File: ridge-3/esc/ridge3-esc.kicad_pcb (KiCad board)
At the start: 6 copper layers, 33.8 x 33.8 mm, 171 parts, among them Q1A AON7934, Q1B AON7934, Q1C AON7934, Q2A AON7934, Q2B AON7934, Q2C AON7934, Q3A AON7934, Q3B AON7934, Q3C AON7934, Q4A AON7934, Q4B AON7934, Q4C AON7934

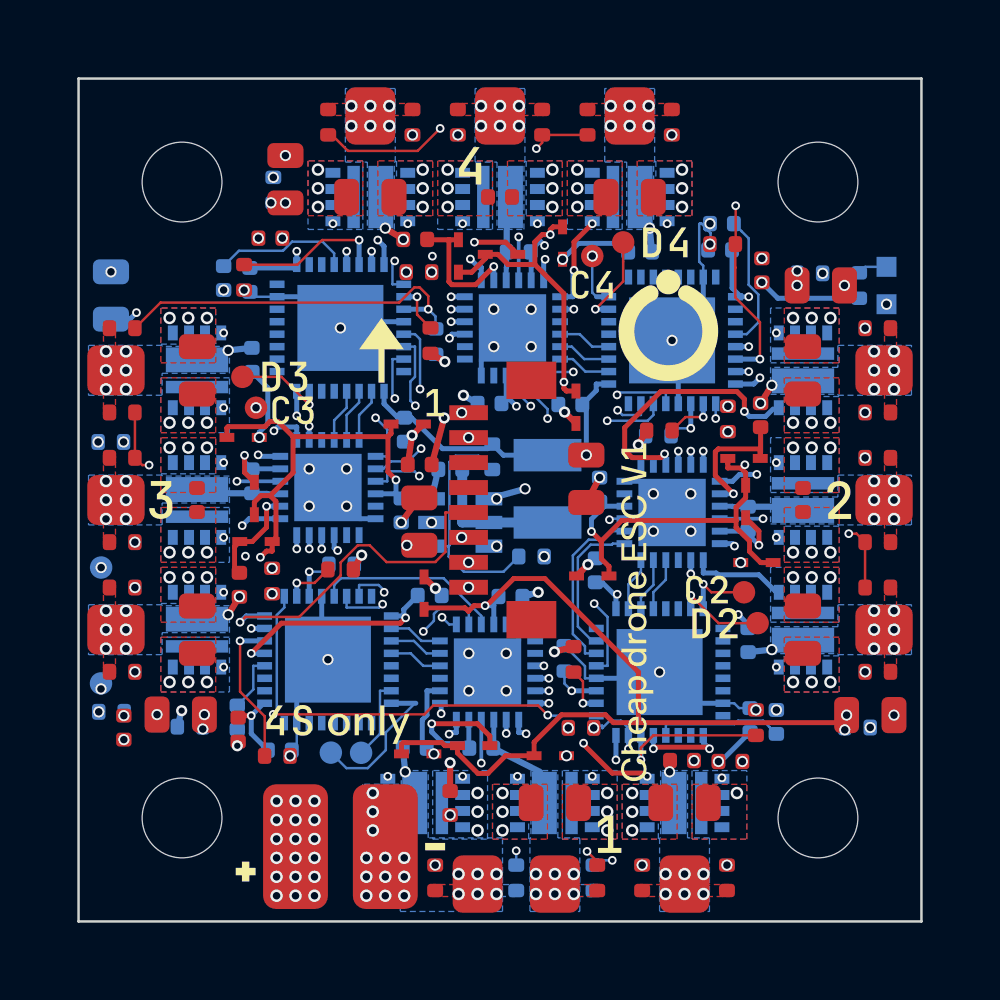
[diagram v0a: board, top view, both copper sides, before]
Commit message: ESC routed to DRC 0/0/0 and installed; panel fiducial check reads real extents
The deterministic run (pipeline.run 'esc', seed as committed) routed the
channel template with 0 nets open, stamped it onto all four channels with
every copy kept, and Freerouting finished the whole board with nothing
left: DRC 0 errors, 0 warnings, 0 unconnected with the silkscreen on.
Installed as esc/ridge3-esc.kicad_pcb with its outputs; the old
cheapdrone-esc images, production files and STEP are gone.

The panel's fiducial keep-out check sized an aperture macro by its
largest parameter; a free-polygon pad's first parameter is its rotation,
so a pad turned 180 degrees counted as a 180 mm disc and "covered" every
bottom fiducial. It now measures each object's real extent (gerbonara
evaluates the macro): region outlines, else bounding boxes.

The ESC's firmware name (RIDGE3_G071) found no room on top; it now goes
on the bottom when the top has none.

Co-Authored-By: Claude Opus 5.5 <noreply@anthropic.com>
Claude-Session: https://claude.ai/code/session_01MaVFAzoExts7u2gmCraXFC
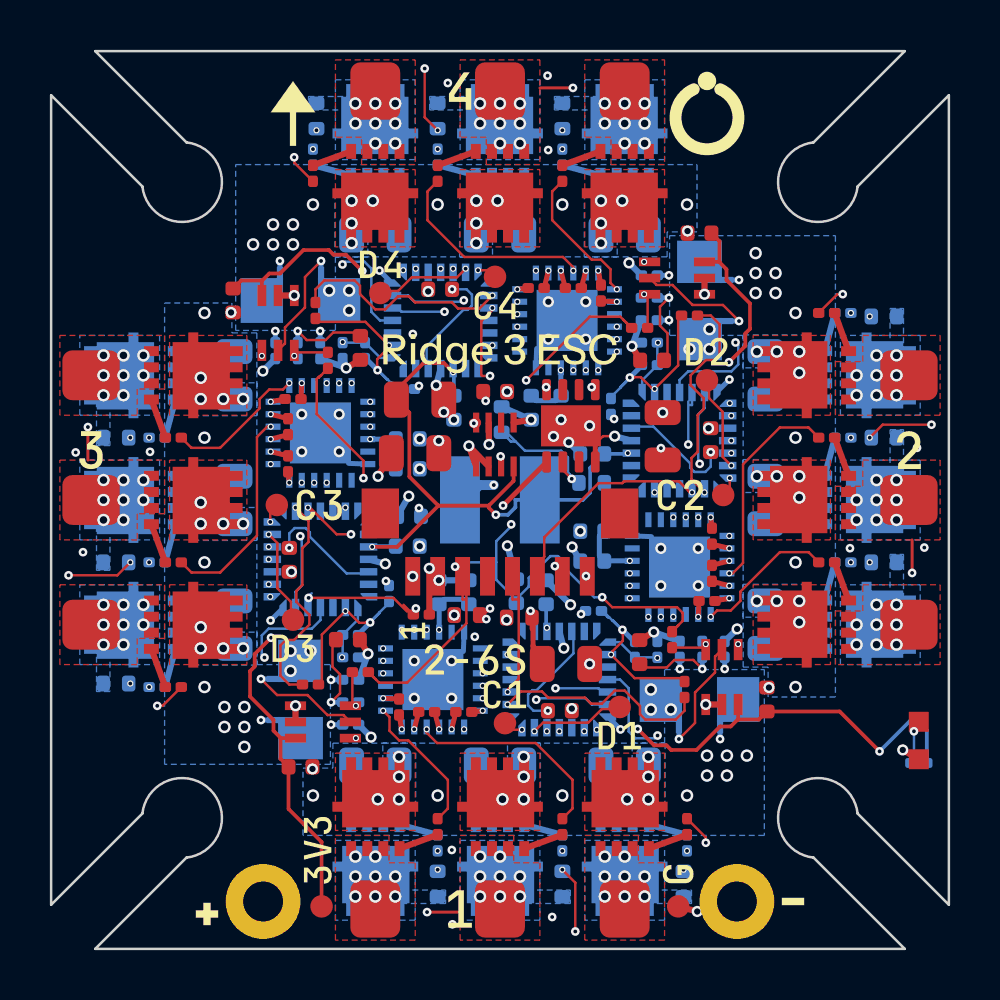
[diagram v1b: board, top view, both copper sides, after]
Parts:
- removed D1, D13, D5, D9: 15V, SOD-523_L1.2-W0.8-LS1.6-RD
- removed D10, D11, D12, D14, D15, D16, D2, D3, D4, D6, D7, D8: RB521S30, SOD-523_L1.2-W0.8-LS1.6-RD
- removed the LED_PWR at (115.5, 91.4)
- removed Q1A, Q1B, Q1C, Q2A, Q2B, Q2C, Q3A, Q3B, Q3C, Q4A, Q4B, Q4C: AON7934, DFN-8_L3.0-W3.0-P0.65-BL_AON7934
- removed the U_BUCK at (98.4, 100.9)
- added C55: 100nF, C_0402_1005Metric, F.Cu at (94.4, 93.9)
- added LED_PWR: RED, LED0603-RD, F.Cu at (116.8, 109.6)
- added Q1AH: TPN2R304PL, TSON-8_L3.1-W3.1-P0.65-LS3.3-BL-EP, F.Cu at (95.0, 112.3)
- added Q1AL: TPN2R304PL, TSON-8_L3.1-W3.1-P0.65-LS3.3-BL-EP, B.Cu at (95.0, 114.7)
- added Q1BH: TPN2R304PL, TSON-8_L3.1-W3.1-P0.65-LS3.3-BL-EP, F.Cu at (100.0, 112.3)
- added Q1BL: TPN2R304PL, TSON-8_L3.1-W3.1-P0.65-LS3.3-BL-EP, B.Cu at (100.0, 114.7)
- added Q1CH: TPN2R304PL, TSON-8_L3.1-W3.1-P0.65-LS3.3-BL-EP, F.Cu at (105.0, 112.3)
- added Q1CL: TPN2R304PL, TSON-8_L3.1-W3.1-P0.65-LS3.3-BL-EP, B.Cu at (105.0, 114.7)
- added Q2AH: TPN2R304PL, TSON-8_L3.1-W3.1-P0.65-LS3.3-BL-EP, F.Cu at (112.3, 105.0)
- added Q2AL: TPN2R304PL, TSON-8_L3.1-W3.1-P0.65-LS3.3-BL-EP, B.Cu at (114.7, 105.0)
- added Q2BH: TPN2R304PL, TSON-8_L3.1-W3.1-P0.65-LS3.3-BL-EP, F.Cu at (112.3, 100.0)
- added Q2BL: TPN2R304PL, TSON-8_L3.1-W3.1-P0.65-LS3.3-BL-EP, B.Cu at (114.7, 100.0)
- added Q2CH: TPN2R304PL, TSON-8_L3.1-W3.1-P0.65-LS3.3-BL-EP, F.Cu at (112.3, 95.0)
- added Q2CL: TPN2R304PL, TSON-8_L3.1-W3.1-P0.65-LS3.3-BL-EP, B.Cu at (114.7, 95.0)
- added Q3AH: TPN2R304PL, TSON-8_L3.1-W3.1-P0.65-LS3.3-BL-EP, F.Cu at (87.7, 95.0)
- added Q3AL: TPN2R304PL, TSON-8_L3.1-W3.1-P0.65-LS3.3-BL-EP, B.Cu at (85.3, 95.0)
- added Q3BH: TPN2R304PL, TSON-8_L3.1-W3.1-P0.65-LS3.3-BL-EP, F.Cu at (87.7, 100.0)
- added Q3BL: TPN2R304PL, TSON-8_L3.1-W3.1-P0.65-LS3.3-BL-EP, B.Cu at (85.3, 100.0)
- added Q3CH: TPN2R304PL, TSON-8_L3.1-W3.1-P0.65-LS3.3-BL-EP, F.Cu at (87.7, 105.0)
- added Q3CL: TPN2R304PL, TSON-8_L3.1-W3.1-P0.65-LS3.3-BL-EP, B.Cu at (85.3, 105.0)
- added Q4AH: TPN2R304PL, TSON-8_L3.1-W3.1-P0.65-LS3.3-BL-EP, F.Cu at (105.0, 87.7)
- added Q4AL: TPN2R304PL, TSON-8_L3.1-W3.1-P0.65-LS3.3-BL-EP, B.Cu at (105.0, 85.3)
- added Q4BH: TPN2R304PL, TSON-8_L3.1-W3.1-P0.65-LS3.3-BL-EP, F.Cu at (100.0, 87.7)
- added Q4BL: TPN2R304PL, TSON-8_L3.1-W3.1-P0.65-LS3.3-BL-EP, B.Cu at (100.0, 85.3)
- added Q4CH: TPN2R304PL, TSON-8_L3.1-W3.1-P0.65-LS3.3-BL-EP, F.Cu at (95.0, 87.7)
- added Q4CL: TPN2R304PL, TSON-8_L3.1-W3.1-P0.65-LS3.3-BL-EP, B.Cu at (95.0, 85.3)
- added R50: 20k, R_0402_1005Metric, B.Cu at (84.6, 102.5)
- added R51: 2k, R_0201_0603Metric, B.Cu at (94.0, 109.0)
- added R52: 10k, R_0201_0603Metric, F.Cu at (92.4, 107.4)
- added R53: 10R, R_0201_0603Metric, F.Cu at (86.9, 107.5)
- added R54: 10R, R_0201_0603Metric, B.Cu at (86.2, 107.5)
- added R55: 20k, R_0402_1005Metric, B.Cu at (84.6, 107.4)
- added R56: 2k, R_0201_0603Metric, B.Cu at (94.0, 106.3)
- added R57: 10k, R_0201_0603Metric, B.Cu at (94.0, 105.4)
- added R58: 1k, R_0201_0603Metric, B.Cu at (94.0, 108.1)
- added R59: 10R, R_0201_0603Metric, F.Cu at (102.5, 86.9)
- added R60: 10R, R_0201_0603Metric, B.Cu at (102.5, 86.2)
- added R61: 20k, R_0402_1005Metric, B.Cu at (102.5, 84.6)
- added R62: 2k, R_0201_0603Metric, B.Cu at (92.8, 94.0)
- added R63: 10k, R_0201_0603Metric, B.Cu at (96.2, 95.5)
- added R64: 10R, R_0201_0603Metric, F.Cu at (97.5, 86.9)
- added R65: 10R, R_0201_0603Metric, B.Cu at (97.5, 86.2)
- added R66: 20k, R_0402_1005Metric, B.Cu at (97.5, 84.6)
- added R67: 2k, R_0201_0603Metric, B.Cu at (91.0, 94.0)
- added R68: 10k, R_0201_0603Metric, F.Cu at (92.6, 92.4)
- added R69: 10R, R_0201_0603Metric, F.Cu at (92.5, 86.9)
- added R70: 10R, R_0201_0603Metric, B.Cu at (92.5, 86.2)
- added R71: 20k, R_0402_1005Metric, B.Cu at (92.6, 84.6)
- added R72: 2k, R_0201_0603Metric, B.Cu at (93.7, 94.0)
- added R73: 10k, R_0201_0603Metric, B.Cu at (94.6, 94.0)
- added R74: 1k, R_0201_0603Metric, B.Cu at (91.9, 94.0)
- added R_SH1: 0.5mR, RES-SMD_1206_HCS1206, B.Cu at (108.0, 108.0)
- added R_SH2: 0.5mR, RES-SMD_1206_HCS1206, B.Cu at (108.0, 92.0)
- added R_SH3: 0.5mR, RES-SMD_1206_HCS1206, B.Cu at (92.0, 108.0)
- added R_SH4: 0.5mR, RES-SMD_1206_HCS1206, B.Cu at (92.0, 92.0)
- added U_BUCK: MAX15062A 3.3V, TDFN-8_L2.0-W2.0-P0.50-BL_MAX15062AATA, F.Cu at (99.8, 97.8)
- added U_CS1: INA186A3, SC-70-6_L2.0-W1.3-P0.65-LS2.1-BL, F.Cu at (108.9, 107.1)
- added U_CS2: INA186A3, SC-70-6_L2.0-W1.3-P0.65-LS2.1-BL, F.Cu at (107.1, 91.1)
- added U_CS3: INA186A3, SC-70-6_L2.0-W1.3-P0.65-LS2.1-BL, F.Cu at (92.9, 108.9)
- added U_CS4: INA186A3, SC-70-6_L2.0-W1.3-P0.65-LS2.1-BL, F.Cu at (91.1, 92.9)
- added U_GVDD: TPS7A1601, VSON-8-1EP_3x3mm_P0.65mm_EP1.65x2.4mm, F.Cu at (102.8, 97.0)
- C1, C11, C23, C35, C47: value 10uF -> 100nF; footprint C_0805_2012Metric -> C_0402_1005Metric; moved to B.Cu
- C10, C22, C34, C46: value 100nF -> 1uF
- C12, C24, C36, C48: value 100nF -> 1uF; footprint C_0402_1005Metric -> C_0201_0603Metric; moved to F.Cu
- C13, C25, C37, C49: value 1uF -> 4.7uF; footprint C_0402_1005Metric -> C_0805_2012Metric
- C14, C26, C38, C50: footprint C_0402_1005Metric -> C_0201_0603Metric; moved to F.Cu
- C15, C27, C39, C51: value 1uF -> 4.7uF; footprint C_0402_1005Metric -> C_0805_2012Metric; moved to B.Cu
- C16, C28, C40, C52: value 10uF -> 1uF; footprint C_0805_2012Metric -> C_0201_0603Metric
- C17, C29, C41, C53: value 10uF -> 4.7uF; moved to B.Cu
- C19, C31, C43, TP_3V3, TP_E1_CLK, TP_E1_DIO, TP_GND: moved to F.Cu
- C2: value 100nF -> 1uF; footprint C_0402_1005Metric -> C_0805_2012Metric
- C20, C32, C44, C8: value 4.7uF -> 100nF
- C21, C33, C45, C9: value 1uF -> 100nF
- C3: value 100nF -> 1uF; moved to F.Cu
- C4: value 22uF -> 10uF
- C5: value 22uF -> 1uF; moved to F.Cu
- C6: value 100nF -> 4.7uF; footprint C_0402_1005Metric -> C_0805_2012Metric
- H1, H2, H3, H4: footprint HOLE_M3 -> MOUNT_M2_SLOT
- L1: value 4.7uH -> 33uH; footprint IND-SMD_L3.0-W3.0_FNR30XXS -> IND-SMD_L4.0-W4.0
- R1: value 100k -> 10k; footprint R_0402_1005Metric -> R_0201_0603Metric; moved to F.Cu
- R10, R20: footprint R_0402_1005Metric -> R_0201_0603Metric
- R11: value 2.2k -> 10R; footprint R_0402_1005Metric -> R_0201_0603Metric
- R12, R21, R32, R37, R43, R48: value 10k -> 10R; footprint R_0402_1005Metric -> R_0201_0603Metric
- R13, R18, R23, R29, R34, R45: value 10k -> 20k; moved to B.Cu
- R14: value 2.2k -> 2k; footprint R_0402_1005Metric -> R_0201_0603Metric; moved to B.Cu
- R15, R31: footprint R_0402_1005Metric -> R_0201_0603Metric; moved to B.Cu
- R16, R27: value 750R -> 10R; footprint R_0402_1005Metric -> R_0201_0603Metric
- R17, R28: value 330R -> 10R; footprint R_0402_1005Metric -> R_0201_0603Metric
- R19, R30: value 2.2k -> 2k; footprint R_0402_1005Metric -> R_0201_0603Metric
- R2: value 22k -> 10k; footprint R_0402_1005Metric -> R_0201_0603Metric; moved to F.Cu
- R22, R33, R44: value 2.2k -> 10R; footprint R_0402_1005Metric -> R_0201_0603Metric; moved to B.Cu
- R24, R35, R40, R46: value 10k -> 2k; footprint R_0402_1005Metric -> R_0201_0603Metric; moved to B.Cu
- R25, R47: value 2.2k -> 10k; footprint R_0402_1005Metric -> R_0201_0603Metric; moved to B.Cu
- R26, R42: value 10k -> 1k; footprint R_0402_1005Metric -> R_0201_0603Metric; moved to B.Cu
- R3: value 1k -> 10k; footprint R_0402_1005Metric -> R_0201_0603Metric; moved to F.Cu
- R36, R41: value 2.2k -> 10k; footprint R_0402_1005Metric -> R_0201_0603Metric
- R38, R49: value 750R -> 10R; footprint R_0402_1005Metric -> R_0201_0603Metric; moved to B.Cu
- R39: value 330R -> 20k
- R4: value 11k -> 10k; footprint R_0402_1005Metric -> R_0201_0603Metric; moved to F.Cu
- R5: value 2k -> 1k; footprint R_0402_1005Metric -> R_0201_0603Metric
- R6: value 330R -> 22R; moved to F.Cu
- R7: value 10k -> 88.7k; moved to B.Cu
- R8: value 2.2k -> 10.2k
- R9: value 10k -> 100k; moved to F.Cu
- U_ESC1, U_ESC2, U_ESC3, U_ESC4: value STM32F051K6U6 -> STM32G071GBU6; footprint UFQFPN-32_L5.0-W5.0-P0.50-BL-EP -> UFQFPN-28_L4.0-W4.0-P0.50-BL
- U_GD1, U_GD2, U_GD3, U_GD4: value JSM6288Q -> DRV8300DRGER; footprint VQFN-24_L4.0-W4.0-P0.50-TL-EP2.7 -> VQFN-24_L4.0-W4.0-P0.50-TL-EP2.5
- moved R5 32.4 mm to (116.8, 110.5)
- moved R29 32.0 mm to (115.4, 102.5), turned to 180 degrees
- moved R34 30.6 mm to (115.4, 97.5), turned to 180 degrees
- moved R37 30.3 mm to (113.1, 92.5)
- moved R32 28.6 mm to (113.1, 97.5)
- moved R28 27.0 mm to (113.8, 102.5), turned to 180 degrees
- moved R35 26.5 mm to (106.0, 91.0), turned to 180 degrees
- moved R3 25.3 mm to (94.4, 106.9), turned to 0 degrees
- moved R39 25.0 mm to (115.4, 92.6), turned to 180 degrees
- moved R17 24.9 mm to (102.5, 113.8), turned to 90 degrees
- moved TP_GND 24.8 mm to (107.1, 116.3), turned to 0 degrees
- moved C6 24.6 mm to (106.5, 97.4), turned to 90 degrees
- moved R49 23.6 mm to (86.2, 102.5), turned to 0 degrees
- moved C5 23.5 mm to (102.6, 106.6), turned to 0 degrees
- moved R46 22.4 mm to (94.0, 107.2), turned to 0 degrees
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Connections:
- net M1_VBB renamed M1_BSTB
- net M2_VBB renamed M2_BSTB
- net M3_VBB renamed M3_BSTB
- net M4_VBB renamed M4_BSTB
- C1 pad 1: VBAT -> CUR
- C10 pad 1: M1_NRST -> GVDD
- C11 pad 1: M1_VCC -> GVDD
- C12 pad 1: M1_VCC -> M1_BSTA
- C12 pad 2: GND -> M1_A
- C13 pad 1: M1_VBA -> VBAT
- C13 pad 2: M1_A -> M1_SRC
- C15 pad 1: M1_VBC -> VBAT
- C15 pad 2: M1_C -> M1_SRC
- C16 pad 1: VBAT -> M1_BSTC
- C16 pad 2: GND -> M1_C
- C17 pad 2: GND -> M1_SRC
- C18 pad 1: VBAT -> +3V3
- C19 pad 1: +3V3 -> M1_ISENSE
- C21 pad 1: +3V3 -> M2_NRST
- C22 pad 1: M2_NRST -> GVDD
- C23 pad 1: M2_VCC -> GVDD
- C24 pad 1: M2_VCC -> M2_BSTA
- C24 pad 2: GND -> M2_A
- C25 pad 1: M2_VBA -> VBAT
- C25 pad 2: M2_A -> M2_SRC
- C27 pad 1: M2_VBC -> VBAT
- C27 pad 2: M2_C -> M2_SRC
- C28 pad 1: VBAT -> M2_BSTC
- C28 pad 2: GND -> M2_C
- C29 pad 2: GND -> M2_SRC
- C3 pad 1: BUCK_CB -> BUCK_VCC
- C3 pad 2: BUCK_SW -> GND
- C30 pad 1: VBAT -> +3V3
- C31 pad 1: +3V3 -> M2_ISENSE
- C33 pad 1: +3V3 -> M3_NRST
- C34 pad 1: M3_NRST -> GVDD
- C35 pad 1: M3_VCC -> GVDD
- C36 pad 1: M3_VCC -> M3_BSTA
- C36 pad 2: GND -> M3_A
- C37 pad 1: M3_VBA -> VBAT
- C37 pad 2: M3_A -> M3_SRC
- C39 pad 1: M3_VBC -> VBAT
- C39 pad 2: M3_C -> M3_SRC
- C40 pad 1: VBAT -> M3_BSTC
- C40 pad 2: GND -> M3_C
- C41 pad 2: GND -> M3_SRC
- C42 pad 1: VBAT -> +3V3
- C43 pad 1: +3V3 -> M3_ISENSE
- C45 pad 1: +3V3 -> M4_NRST
- C46 pad 1: M4_NRST -> GVDD
- C47 pad 1: M4_VCC -> GVDD
- C48 pad 1: M4_VCC -> M4_BSTA
- C48 pad 2: GND -> M4_A
- C49 pad 1: M4_VBA -> VBAT
- C49 pad 2: M4_A -> M4_SRC
- C5 pad 1: +3V3 -> GVDD_IN
- C51 pad 1: M4_VBC -> VBAT
- C51 pad 2: M4_C -> M4_SRC
- C52 pad 1: VBAT -> M4_BSTC
- C52 pad 2: GND -> M4_C
- C53 pad 2: GND -> M4_SRC
- C54 pad 1: VBAT -> +3V3
- C6 pad 1: ESC_VSENSE -> GVDD
- C7 pad 1: +3V3 -> ESC_VSENSE
- C9 pad 1: +3V3 -> M1_NRST
- J_FC pad 3: (no net) -> CUR
- L1 pad 1: BUCK_SW -> BUCK_LX
- R1 pad 1: +3V3 -> M1_IOUT
- R1 pad 2: BUCK_FB -> CUR
- R10 pad 1: M1_B -> ESC_VSENSE
- R10 pad 2: M1_CMP_B -> GND
- R11 pad 1: M1_CMP_B -> M1_GHA_D
- R11 pad 2: GND -> M1_GHA
- R12 pad 1: M1_B -> M1_GLA_D
- R12 pad 2: M1_NEUTRAL -> M1_GLA
- R13 pad 1: M1_C -> M1_A
- R13 pad 2: M1_CMP_C -> M1_CMP_A
- R14 pad 1: M1_CMP_C -> M1_CMP_A
- R15 pad 1: M1_C -> M1_CMP_A
- R16 pad 1: M1_NEUTRAL -> M1_GHB_D
- R16 pad 2: GND -> M1_GHB
- R17 pad 1: VBAT -> M1_GLB_D
- R17 pad 2: M2_VCC -> M1_GLB
- R18 pad 1: M2_A -> M1_B
- R18 pad 2: M2_CMP_A -> M1_CMP_B
- R19 pad 1: M2_CMP_A -> M1_CMP_B
- R2 pad 1: BUCK_FB -> M2_IOUT
- R2 pad 2: GND -> CUR
- R20 pad 1: M2_A -> M1_CMP_B
- R20 pad 2: M2_NEUTRAL -> M1_NEUTRAL
- R21 pad 1: M2_B -> M1_GHC_D
- R21 pad 2: M2_CMP_B -> M1_GHC
- R22 pad 1: M2_CMP_B -> M1_GLC_D
- R22 pad 2: GND -> M1_GLC
- R23 pad 1: M2_B -> M1_C
- R23 pad 2: M2_NEUTRAL -> M1_CMP_C
- R24 pad 1: M2_C -> M1_CMP_C
- R24 pad 2: M2_CMP_C -> GND
- R25 pad 1: M2_CMP_C -> M1_CMP_C
- R25 pad 2: GND -> M1_NEUTRAL
- R26 pad 1: M2_C -> M1_IOUT
- R26 pad 2: M2_NEUTRAL -> M1_ISENSE
- R27 pad 1: M2_NEUTRAL -> M2_GHA_D
- R27 pad 2: GND -> M2_GHA
- R28 pad 1: VBAT -> M2_GLA_D
- R28 pad 2: M3_VCC -> M2_GLA
- R29 pad 1: M3_A -> M2_A
- R29 pad 2: M3_CMP_A -> M2_CMP_A
- R3 pad 1: +3V3 -> M3_IOUT
- R3 pad 2: LED_PWR_A -> CUR
- R30 pad 1: M3_CMP_A -> M2_CMP_A
- R31 pad 1: M3_A -> M2_CMP_A
- R31 pad 2: M3_NEUTRAL -> M2_NEUTRAL
- R32 pad 1: M3_B -> M2_GHB_D
- R32 pad 2: M3_CMP_B -> M2_GHB
- R33 pad 1: M3_CMP_B -> M2_GLB_D
- R33 pad 2: GND -> M2_GLB
- R34 pad 1: M3_B -> M2_B
- R34 pad 2: M3_NEUTRAL -> M2_CMP_B
- R35 pad 1: M3_C -> M2_CMP_B
- R35 pad 2: M3_CMP_C -> GND
- R36 pad 1: M3_CMP_C -> M2_CMP_B
- R36 pad 2: GND -> M2_NEUTRAL
- R37 pad 1: M3_C -> M2_GHC_D
- R37 pad 2: M3_NEUTRAL -> M2_GHC
- R38 pad 1: M3_NEUTRAL -> M2_GLC_D
- R38 pad 2: GND -> M2_GLC
- R39 pad 1: VBAT -> M2_C
- R39 pad 2: M4_VCC -> M2_CMP_C
- R4 pad 1: VBAT -> M4_IOUT
- R4 pad 2: ESC_VSENSE -> CUR
- R40 pad 1: M4_A -> M2_CMP_C
- R40 pad 2: M4_CMP_A -> GND
- R41 pad 1: M4_CMP_A -> M2_CMP_C
- R41 pad 2: GND -> M2_NEUTRAL
- R42 pad 1: M4_A -> M2_IOUT
- R42 pad 2: M4_NEUTRAL -> M2_ISENSE
- R43 pad 1: M4_B -> M3_GHA_D
- R43 pad 2: M4_CMP_B -> M3_GHA
- R44 pad 1: M4_CMP_B -> M3_GLA_D
- R44 pad 2: GND -> M3_GLA
- R45 pad 1: M4_B -> M3_A
- R45 pad 2: M4_NEUTRAL -> M3_CMP_A
- R46 pad 1: M4_C -> M3_CMP_A
- R46 pad 2: M4_CMP_C -> GND
- R47 pad 1: M4_CMP_C -> M3_CMP_A
- R47 pad 2: GND -> M3_NEUTRAL
- R48 pad 1: M4_C -> M3_GHB_D
- R48 pad 2: M4_NEUTRAL -> M3_GHB
- R49 pad 1: M4_NEUTRAL -> M3_GLB_D
- R49 pad 2: GND -> M3_GLB
- R5 pad 1: ESC_VSENSE -> +3V3
- R5 pad 2: GND -> LED_PWR_A
- R6 pad 2: M1_VCC -> GVDD_IN
- R7 pad 1: M1_A -> GVDD
- R7 pad 2: M1_CMP_A -> GVDD_FB
- R8 pad 1: M1_CMP_A -> GVDD_FB
- R9 pad 1: M1_A -> VBAT
- R9 pad 2: M1_NEUTRAL -> ESC_VSENSE
- U_ESC1 pad 1: +3V3 -> (no net)
- U_ESC1 pad 10: M1_CMP_B -> (no net)
- U_ESC1 pad 11: M1_CMP_A -> M1_ISENSE
- U_ESC1 pad 12: GND -> ESC_VSENSE
- U_ESC1 pad 16: (no net) -> M1_HC
- U_ESC1 pad 17: +3V3 -> (no net)
- U_ESC1 pad 18: M1_HC -> M1_HB
- U_ESC1 pad 19: M1_HB -> M1_HA
- U_ESC1 pad 20: M1_HA -> M1_SWDIO
- U_ESC1 pad 21: (no net) -> M1_SWCLK
- U_ESC1 pad 23: M1_SWDIO -> M1_CMP_B
- U_ESC1 pad 24: M1_SWCLK -> M1_SIG
- U_ESC1 pad 27: (no net) -> M1_CMP_A
- U_ESC1 pad 3: (no net) -> +3V3
- U_ESC1 pad 4: M1_NRST -> GND
- U_ESC1 pad 5: +3V3 -> M1_NRST
- U_ESC1 pad 6: M1_CMP_C -> (no net)
- U_ESC1 pad 7: M1_NEUTRAL -> (no net)
- U_ESC1 pad 8: M1_SIG -> M1_CMP_C
- U_ESC1 pad 9: ESC_VSENSE -> M1_NEUTRAL
- U_ESC2 pad 1: +3V3 -> (no net)
- U_ESC2 pad 10: M2_CMP_B -> (no net)
- U_ESC2 pad 11: M2_CMP_A -> M2_ISENSE
- U_ESC2 pad 12: GND -> ESC_VSENSE
- U_ESC2 pad 16: (no net) -> M2_HC
- U_ESC2 pad 17: +3V3 -> (no net)
- U_ESC2 pad 18: M2_HC -> M2_HB
- U_ESC2 pad 19: M2_HB -> M2_HA
- U_ESC2 pad 20: M2_HA -> M2_SWDIO
- U_ESC2 pad 21: (no net) -> M2_SWCLK
- U_ESC2 pad 23: M2_SWDIO -> M2_CMP_B
- U_ESC2 pad 24: M2_SWCLK -> M2_SIG
- U_ESC2 pad 27: (no net) -> M2_CMP_A
- U_ESC2 pad 3: (no net) -> +3V3
- U_ESC2 pad 4: M2_NRST -> GND
- U_ESC2 pad 5: +3V3 -> M2_NRST
- U_ESC2 pad 6: M2_CMP_C -> (no net)
- U_ESC2 pad 7: M2_NEUTRAL -> (no net)
- U_ESC2 pad 8: M2_SIG -> M2_CMP_C
- U_ESC2 pad 9: ESC_VSENSE -> M2_NEUTRAL
- U_ESC3 pad 1: +3V3 -> (no net)
- U_ESC3 pad 10: M3_CMP_B -> (no net)
- U_ESC3 pad 11: M3_CMP_A -> M3_ISENSE
- U_ESC3 pad 12: GND -> ESC_VSENSE
- U_ESC3 pad 16: (no net) -> M3_HC
- U_ESC3 pad 17: +3V3 -> (no net)
- U_ESC3 pad 18: M3_HC -> M3_HB
- U_ESC3 pad 19: M3_HB -> M3_HA
- U_ESC3 pad 20: M3_HA -> M3_SWDIO
- U_ESC3 pad 21: (no net) -> M3_SWCLK
- U_ESC3 pad 23: M3_SWDIO -> M3_CMP_B
- U_ESC3 pad 24: M3_SWCLK -> M3_SIG
- U_ESC3 pad 27: (no net) -> M3_CMP_A
- U_ESC3 pad 3: (no net) -> +3V3
- U_ESC3 pad 4: M3_NRST -> GND
- U_ESC3 pad 5: +3V3 -> M3_NRST
- U_ESC3 pad 6: M3_CMP_C -> (no net)
- U_ESC3 pad 7: M3_NEUTRAL -> (no net)
- U_ESC3 pad 8: M3_SIG -> M3_CMP_C
- U_ESC3 pad 9: ESC_VSENSE -> M3_NEUTRAL
- U_ESC4 pad 1: +3V3 -> (no net)
- U_ESC4 pad 10: M4_CMP_B -> (no net)
- U_ESC4 pad 11: M4_CMP_A -> M4_ISENSE
- U_ESC4 pad 12: GND -> ESC_VSENSE
- U_ESC4 pad 16: (no net) -> M4_HC
- U_ESC4 pad 17: +3V3 -> (no net)
- U_ESC4 pad 18: M4_HC -> M4_HB
- U_ESC4 pad 19: M4_HB -> M4_HA
- U_ESC4 pad 20: M4_HA -> M4_SWDIO
- U_ESC4 pad 21: (no net) -> M4_SWCLK
- U_ESC4 pad 23: M4_SWDIO -> M4_CMP_B
- U_ESC4 pad 24: M4_SWCLK -> M4_SIG
- U_ESC4 pad 27: (no net) -> M4_CMP_A
- U_ESC4 pad 3: (no net) -> +3V3
- U_ESC4 pad 4: M4_NRST -> GND
- U_ESC4 pad 5: +3V3 -> M4_NRST
- U_ESC4 pad 6: M4_CMP_C -> (no net)
- U_ESC4 pad 7: M4_NEUTRAL -> (no net)
- U_ESC4 pad 8: M4_SIG -> M4_CMP_C
- U_ESC4 pad 9: ESC_VSENSE -> M4_NEUTRAL
- U_GD1 pad 10: M1_GLB -> M1_GLB_D
- U_GD1 pad 11: M1_GLA -> M1_GLA_D
- U_GD1 pad 13: M1_GHC -> M1_GHC_D
- U_GD1 pad 14: M1_VBC -> M1_BSTC
- U_GD1 pad 16: M1_GHB -> M1_GHB_D
- U_GD1 pad 19: M1_GHA -> M1_GHA_D
- U_GD1 pad 20: M1_VBA -> M1_BSTA
- U_GD1 pad 4: M1_VCC -> GVDD
- U_GD1 pad 9: M1_GLC -> M1_GLC_D
- U_GD2 pad 10: M2_GLB -> M2_GLB_D
- U_GD2 pad 11: M2_GLA -> M2_GLA_D
- U_GD2 pad 13: M2_GHC -> M2_GHC_D
- U_GD2 pad 14: M2_VBC -> M2_BSTC
- U_GD2 pad 16: M2_GHB -> M2_GHB_D
- U_GD2 pad 19: M2_GHA -> M2_GHA_D
- U_GD2 pad 20: M2_VBA -> M2_BSTA
- U_GD2 pad 4: M2_VCC -> GVDD
- U_GD2 pad 9: M2_GLC -> M2_GLC_D
- U_GD3 pad 10: M3_GLB -> M3_GLB_D
- U_GD3 pad 11: M3_GLA -> M3_GLA_D
- U_GD3 pad 13: M3_GHC -> M3_GHC_D
- U_GD3 pad 14: M3_VBC -> M3_BSTC
- U_GD3 pad 16: M3_GHB -> M3_GHB_D
- U_GD3 pad 19: M3_GHA -> M3_GHA_D
- U_GD3 pad 20: M3_VBA -> M3_BSTA
- U_GD3 pad 4: M3_VCC -> GVDD
- U_GD3 pad 9: M3_GLC -> M3_GLC_D
- U_GD4 pad 10: M4_GLB -> M4_GLB_D
- U_GD4 pad 11: M4_GLA -> M4_GLA_D
- U_GD4 pad 13: M4_GHC -> M4_GHC_D
- U_GD4 pad 14: M4_VBC -> M4_BSTC
- U_GD4 pad 16: M4_GHB -> M4_GHB_D
- U_GD4 pad 19: M4_GHA -> M4_GHA_D
- U_GD4 pad 20: M4_VBA -> M4_BSTA
- U_GD4 pad 4: M4_VCC -> GVDD
- U_GD4 pad 9: M4_GLC -> M4_GLC_D
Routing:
- net GVDD: track 0.00 -> 53.6 mm, vias 0 -> 7
- net CUR: track 0.00 -> 45.4 mm, vias 0 -> 5
- net M1_VCC: track 35.3 -> 0.00 mm, vias 3 -> 0
- net M4_VCC: track 30.2 -> 0.00 mm, vias 5 -> 0
- net M3_VCC: track 29.2 -> 0.00 mm, vias 4 -> 0
- net M2_VCC: track 25.6 -> 0.00 mm, vias 4 -> 0
- net ESC_VSENSE: track 70.6 -> 49.2 mm, vias 6 -> 8
- net M2_NEUTRAL: track 27.9 -> 7.11 mm, vias 4 -> 2
- net M3_NEUTRAL: track 27.5 -> 7.11 mm, vias 4 -> 2
- net M1_NEUTRAL: track 27.4 -> 7.29 mm, vias 5 -> 2
- net M2_GHC_D: track 0.00 -> 18.5 mm, vias 0 -> 3
- net M1_GHC_D: track 0.00 -> 18.5 mm, vias 0 -> 3
- net M4_GHC_D: track 0.00 -> 18.5 mm, vias 0 -> 3
- net M3_GHC_D: track 0.00 -> 18.5 mm, vias 0 -> 3
- net M1_GLC_D: track 0.00 -> 18.2 mm, vias 0 -> 3
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- added copper zone on B.Cu, net M1_SRC
- added copper zone on In3.Cu, net M1_SRC
- added copper zone on B.Cu, net M2_SRC
- added copper zone on In3.Cu, net M2_SRC
- added copper zone on B.Cu, net M3_SRC
- added copper zone on In3.Cu, net M3_SRC
- added copper zone on B.Cu, net M4_SRC
- added copper zone on In3.Cu, net M4_SRC
- removed copper zone on B.Cu, net GND
- removed copper zone on F.Cu, net GND
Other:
- board size 33.8 x 33.8 mm -> 36 x 36 mm
- rule pad_to_mask_clearance: 0.05 -> 0.04
